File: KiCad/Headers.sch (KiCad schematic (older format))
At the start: 9 parts, among them CON601 AVR-JTAG-10, J601 ISP0, J602 ISP1, J603 CONN_01X02, J604 CONN_01X02, J605 CONN_01X02, J606 CONN_01X02, J607 CONN_01X03, J608 CONN_01X03

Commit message: More routing
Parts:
- CON601: footprint Pin_Headers:Pin_Header_Straight_2x06_Pitch2.54mm -> Pin_Headers:Pin_Header_Straight_2x05_Pitch2.54mm
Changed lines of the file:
@@
 F 0 "CON601" H 4424 1755 50  0000 C CNN
 F 1 "AVR-JTAG-10" H 4424 1664 50  0000 C CNN
-F 2 "Pin_Headers:Pin_Header_Straight_2x06_Pitch2.54mm" V 3880 1320 50  0001 C CNN
+F 2 "Pin_Headers:Pin_Header_Straight_2x05_Pitch2.54mm" V 3880 1320 50  0001 C CNN
 F 3 "" H 4450 1300 50  0001 C CNN
 	1    4450 1300

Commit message: Starting another routing pass
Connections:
- net GPIO/1UART0_TX renamed GPIO1/UART0_TX
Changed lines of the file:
@@
 $EndComp
 $Comp
-L GND #PWR0135
+L GND #PWR0133
 U 1 1 5924B01B
 P 4900 1500
-F 0 "#PWR0135" H 4900 1250 50  0001 C CNN
+F 0 "#PWR0133" H 4900 1250 50  0001 C CNN
 F 1 "GND" V 4905 1372 50  0000 R CNN
 F 2 "" H 4900 1500 50  0001 C CNN
@@
 NoConn ~ 4500 1400
 $Comp
-L GND #PWR0136
+L GND #PWR0134
 U 1 1 5924B02F
 P 4850 1100
-F 0 "#PWR0136" H 4850 850 50  0001 C CNN
+F 0 "#PWR0134" H 4850 850 50  0001 C CNN
 F 1 "GND" V 4855 972 50  0000 R CNN
 F 2 "" H 4850 1100 50  0001 C CNN
@@
 $EndComp
 $Comp
-L +3V3 #PWR0137
+L +3V3 #PWR0135
 U 1 1 5924B035
 P 4850 1200
-F 0 "#PWR0137" H 4850 1050 50  0001 C CNN
+F 0 "#PWR0135" H 4850 1050 50  0001 C CNN
 F 1 "+3V3" V 4865 1328 50  0000 L CNN
 F 2 "" H 4850 1200 50  0001 C CNN
@@
 GPIO17/UART2_TX
 Text GLabel 5450 2800 1    60   Input ~ 0
-GPIO/1UART0_TX
+GPIO1/UART0_TX
 Text GLabel 5300 2800 1    60   Input ~ 0
 GPIO3/UART0_RX
 $Comp
-L GND #PWR0138
+L GND #PWR0136
 U 1 1 59270647
 P 3050 2950
-F 0 "#PWR0138" H 3050 2700 50  0001 C CNN
+F 0 "#PWR0136" H 3050 2700 50  0001 C CNN
 F 1 "GND" V 3055 2822 50  0000 R CNN
 F 2 "" H 3050 2950 50  0001 C CNN
@@
 	3550 2600 3550 2950
 $Comp
-L GND #PWR0139
+L GND #PWR0137
 U 1 1 59270781
 P 3650 2950
-F 0 "#PWR0139" H 3650 2700 50  0001 C CNN
+F 0 "#PWR0137" H 3650 2700 50  0001 C CNN
 F 1 "GND" V 3655 2822 50  0000 R CNN
 F 2 "" H 3650 2950 50  0001 C CNN
@@
 	4150 2600 4150 2950
 $Comp
-L GND #PWR0140
+L GND #PWR0138
 U 1 1 59270905
 P 4250 2950
-F 0 "#PWR0140" H 4250 2700 50  0001 C CNN
+F 0 "#PWR0138" H 4250 2700 50  0001 C CNN
 F 1 "GND" V 4255 2822 50  0000 R CNN
 F 2 "" H 4250 2950 50  0001 C CNN
@@
 	4800 2600 4800 2950
 $Comp
-L GND #PWR0141
+L GND #PWR0139
 U 1 1 59270936
 P 4900 2950
-F 0 "#PWR0141" H 4900 2700 50  0001 C CNN
+F 0 "#PWR0139" H 4900 2700 50  0001 C CNN
 F 1 "GND" V 4905 2822 50  0000 R CNN
 F 2 "" H 4900 2950 50  0001 C CNN
@@
 $EndComp
 $Comp
-L GND #PWR0142
+L GND #PWR0140
 U 1 1 59271A0B
 P 5550 2950
-F 0 "#PWR0142" H 5550 2700 50  0001 C CNN
+F 0 "#PWR0140" H 5550 2700 50  0001 C CNN
 F 1 "GND" V 5555 2822 50  0000 R CNN
 F 2 "" H 5550 2950 50  0001 C CNN
@@
 	5900 2900 5900 2800
 $Comp
-L GND #PWR0143
+L GND #PWR0141
 U 1 1 59271B4E
 P 6150 2950
-F 0 "#PWR0143" H 6150 2700 50  0001 C CNN
+F 0 "#PWR0141" H 6150 2700 50  0001 C CNN
 F 1 "GND" V 6155 2822 50  0000 R CNN
 F 2 "" H 6150 2950 50  0001 C CNN

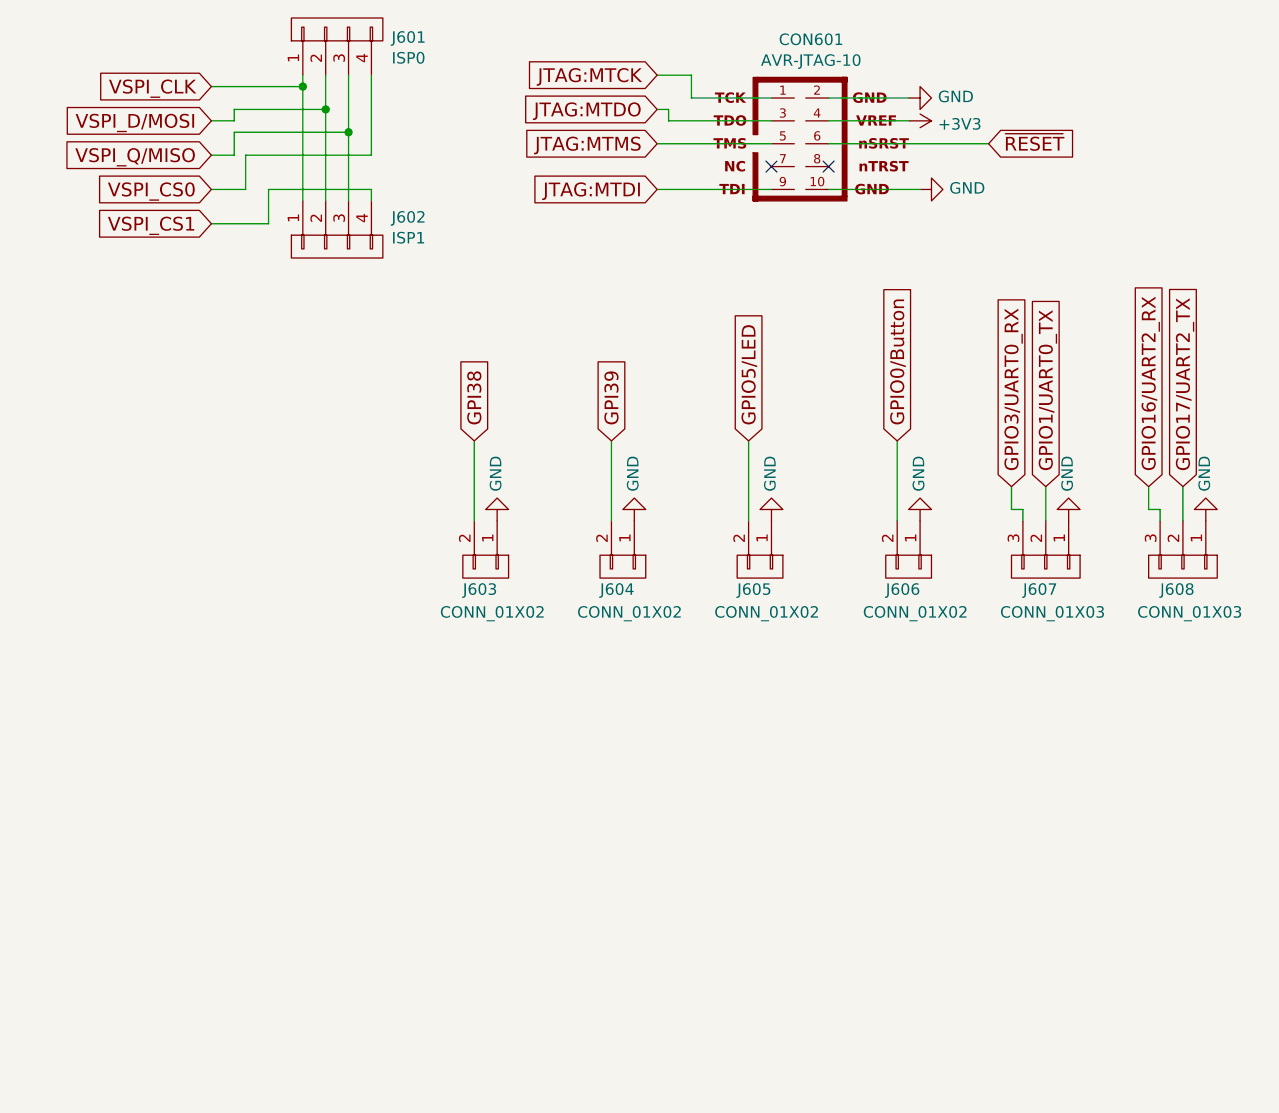
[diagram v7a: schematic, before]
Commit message: Added pullups for JTAG
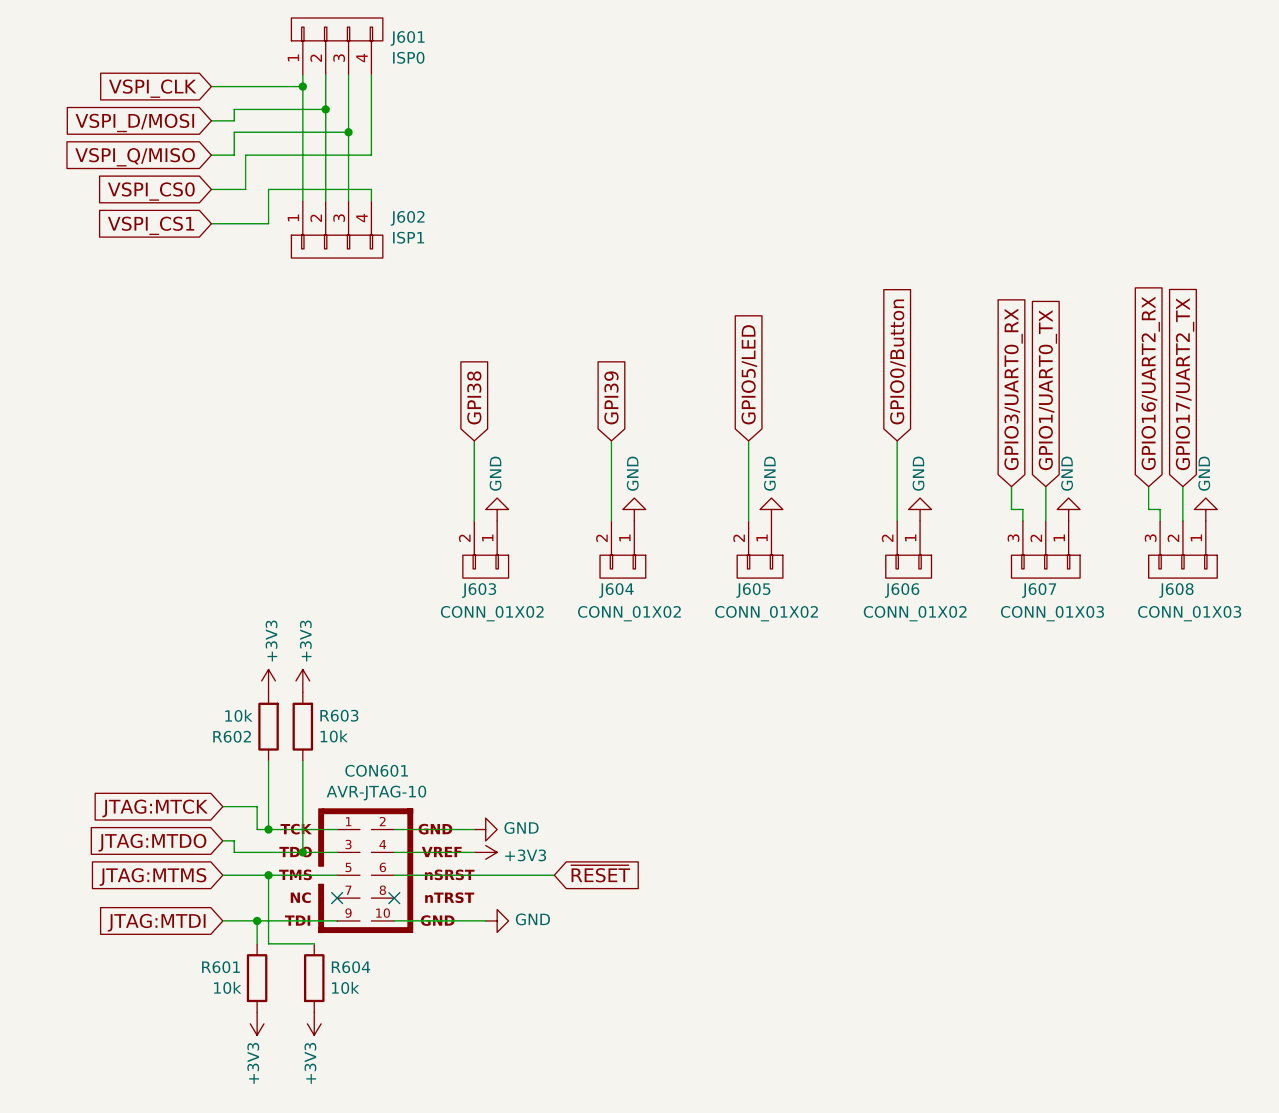
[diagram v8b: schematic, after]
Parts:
- added R601, R602, R603, R604: 10k, Resistors_SMD:R_0805, symbol R
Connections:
- net +3V3: now also R601.2, R602.2, R603.2, R604.2
- net JTAG:MTCK: now also R602.1
- net JTAG:MTDI: now also R601.1
- net JTAG:MTDO: now also R603.1
- net JTAG:MTMS: now also R604.1
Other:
- moved on the sheet: CON601
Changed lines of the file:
@@
 	0    -1   1    0
 $EndComp
-Text GLabel 3750 1500 0    60   Input ~ 0
+Text GLabel 1850 4700 0    60   Input ~ 0
 JTAG:MTDI
-Text GLabel 3750 1150 0    60   Input ~ 0
+Text GLabel 1850 4350 0    60   Input ~ 0
 JTAG:MTDO
-Text GLabel 3750 1000 0    60   Input ~ 0
+Text GLabel 1850 4200 0    60   Input ~ 0
 JTAG:MTCK
-Text GLabel 3750 1300 0    60   Input ~ 0
+Text GLabel 1850 4500 0    60   Input ~ 0
 JTAG:MTMS
-Text GLabel 5200 1300 2    60   Input ~ 0
+Text GLabel 3300 4500 2    60   Input ~ 0
 ~RESET
 $Comp
 L AVR-JTAG-10 CON601
 U 1 1 5924B014
-P 4450 1300
-F 0 "CON601" H 4424 1755 50  0000 C CNN
-F 1 "AVR-JTAG-10" H 4424 1664 50  0000 C CNN
-F 2 "Pin_Headers:Pin_Header_Straight_2x05_Pitch2.54mm" V 3880 1320 50  0001 C CNN
-F 3 "" H 4450 1300 50  0001 C CNN
-	1    4450 1300
-	1    0    0    -1
-$EndComp
-$Comp
-L GND #PWR0133
+P 2550 4500
+F 0 "CON601" H 2524 4955 50  0000 C CNN
+F 1 "AVR-JTAG-10" H 2524 4864 50  0000 C CNN
+F 2 "Pin_Headers:Pin_Header_Straight_2x05_Pitch2.54mm" V 1980 4520 50  0001 C CNN
+F 3 "" H 2550 4500 50  0001 C CNN
+	1    2550 4500
+	1    0    0    -1
+$EndComp
+$Comp
+L GND #PWR607
 U 1 1 5924B01B
-P 4900 1500
-F 0 "#PWR0133" H 4900 1250 50  0001 C CNN
-F 1 "GND" V 4905 1372 50  0000 R CNN
-F 2 "" H 4900 1500 50  0001 C CNN
-F 3 "" H 4900 1500 50  0001 C CNN
-	1    4900 1500
+P 3000 4700
+F 0 "#PWR607" H 3000 4450 50  0001 C CNN
+F 1 "GND" V 3005 4572 50  0000 R CNN
+F 2 "" H 3000 4700 50  0001 C CNN
+F 3 "" H 3000 4700 50  0001 C CNN
+	1    3000 4700
 	0    -1   -1   0
 $EndComp
-NoConn ~ 4250 1400
-NoConn ~ 4500 1400
-$Comp
-L GND #PWR0134
+NoConn ~ 2350 4600
+NoConn ~ 2600 4600
+$Comp
+L GND #PWR605
 U 1 1 5924B02F
-P 4850 1100
-F 0 "#PWR0134" H 4850 850 50  0001 C CNN
-F 1 "GND" V 4855 972 50  0000 R CNN
-F 2 "" H 4850 1100 50  0001 C CNN
-F 3 "" H 4850 1100 50  0001 C CNN
-	1    4850 1100
+P 2950 4300
+F 0 "#PWR605" H 2950 4050 50  0001 C CNN
+F 1 "GND" V 2955 4172 50  0000 R CNN
+F 2 "" H 2950 4300 50  0001 C CNN
+F 3 "" H 2950 4300 50  0001 C CNN
+	1    2950 4300
 	0    -1   -1   0
 $EndComp
 $Comp
-L +3V3 #PWR0135
+L +3V3 #PWR606
 U 1 1 5924B035
-P 4850 1200
-F 0 "#PWR0135" H 4850 1050 50  0001 C CNN
-F 1 "+3V3" V 4865 1328 50  0000 L CNN
-F 2 "" H 4850 1200 50  0001 C CNN
-F 3 "" H 4850 1200 50  0001 C CNN
-	1    4850 1200
+P 2950 4400
+F 0 "#PWR606" H 2950 4250 50  0001 C CNN
+F 1 "+3V3" V 2965 4528 50  0000 L CNN
+F 2 "" H 2950 4400 50  0001 C CNN
+F 3 "" H 2950 4400 50  0001 C CNN
+	1    2950 4400
 	0    1    1    0
 $EndComp
@@
 GPIO3/UART0_RX
 $Comp
-L GND #PWR0136
+L GND #PWR608
 U 1 1 59270647
 P 3050 2950
-F 0 "#PWR0136" H 3050 2700 50  0001 C CNN
+F 0 "#PWR608" H 3050 2700 50  0001 C CNN
 F 1 "GND" V 3055 2822 50  0000 R CNN
 F 2 "" H 3050 2950 50  0001 C CNN
@@
 	2500 1500 2500 1550
 Wire Wire Line
-	4500 1300 5200 1300
-Wire Wire Line
-	3900 1100 4250 1100
-Wire Wire Line
-	4500 1500 4900 1500
-Wire Wire Line
-	4850 1100 4500 1100
-Wire Wire Line
-	3750 1500 4250 1500
-Wire Wire Line
-	3750 1300 4250 1300
-Wire Wire Line
-	3800 1200 4250 1200
-Wire Wire Line
-	4850 1200 4500 1200
-Wire Wire Line
-	3900 1100 3900 1000
-Wire Wire Line
-	3900 1000 3750 1000
-Wire Wire Line
-	3800 1150 3750 1150
-Wire Wire Line
-	3800 1200 3800 1150
+	2600 4500 3300 4500
+Wire Wire Line
+	2000 4300 2350 4300
+Wire Wire Line
+	2600 4700 3000 4700
+Wire Wire Line
+	2950 4300 2600 4300
+Wire Wire Line
+	1850 4700 2350 4700
+Wire Wire Line
+	1850 4500 2350 4500
+Wire Wire Line
+	1900 4400 2350 4400
+Wire Wire Line
+	2950 4400 2600 4400
+Wire Wire Line
+	2000 4300 2000 4200
+Wire Wire Line
+	2000 4200 1850 4200
+Wire Wire Line
+	1900 4350 1850 4350
+Wire Wire Line
+	1900 4400 1900 4350
 Wire Wire Line
 	2950 2950 2950 2600
@@
 	3550 2600 3550 2950
 $Comp
-L GND #PWR0137
+L GND #PWR609
 U 1 1 59270781
 P 3650 2950
-F 0 "#PWR0137" H 3650 2700 50  0001 C CNN
+F 0 "#PWR609" H 3650 2700 50  0001 C CNN
 F 1 "GND" V 3655 2822 50  0000 R CNN
 F 2 "" H 3650 2950 50  0001 C CNN
@@
 	4150 2600 4150 2950
 $Comp
-L GND #PWR0138
+L GND #PWR610
 U 1 1 59270905
 P 4250 2950
-F 0 "#PWR0138" H 4250 2700 50  0001 C CNN
+F 0 "#PWR610" H 4250 2700 50  0001 C CNN
 F 1 "GND" V 4255 2822 50  0000 R CNN
 F 2 "" H 4250 2950 50  0001 C CNN
@@
 	4800 2600 4800 2950
 $Comp
-L GND #PWR0139
+L GND #PWR611
 U 1 1 59270936
 P 4900 2950
-F 0 "#PWR0139" H 4900 2700 50  0001 C CNN
+F 0 "#PWR611" H 4900 2700 50  0001 C CNN
 F 1 "GND" V 4905 2822 50  0000 R CNN
 F 2 "" H 4900 2950 50  0001 C CNN
@@
 $EndComp
 $Comp
-L GND #PWR0140
+L GND #PWR612
 U 1 1 59271A0B
 P 5550 2950
-F 0 "#PWR0140" H 5550 2700 50  0001 C CNN
+F 0 "#PWR612" H 5550 2700 50  0001 C CNN
 F 1 "GND" V 5555 2822 50  0000 R CNN
 F 2 "" H 5550 2950 50  0001 C CNN
@@
 	5900 2900 5900 2800
 $Comp
-L GND #PWR0141
+L GND #PWR613
 U 1 1 59271B4E
 P 6150 2950
-F 0 "#PWR0141" H 6150 2700 50  0001 C CNN
+F 0 "#PWR613" H 6150 2700 50  0001 C CNN
 F 1 "GND" V 6155 2822 50  0000 R CNN
 F 2 "" H 6150 2950 50  0001 C CNN
@@
 	-1   0    0    1
 $EndComp
+$Comp
+L R R601
+U 1 1 594046CD
+P 2000 4950
+F 0 "R601" H 1931 4996 50  0000 R CNN
+F 1 "10k" H 1931 4905 50  0000 R CNN
+F 2 "Resistors_SMD:R_0805" V 1930 4950 50  0001 C CNN
+F 3 "" H 2000 4950 50  0001 C CNN
+	1    2000 4950
+	1    0    0    -1
+$EndComp
+Wire Wire Line
+	2000 4800 2000 4700
+Connection ~ 2000 4700
+$Comp
+L +3V3 #PWR601
+U 1 1 5940481C
+P 2000 5100
+F 0 "#PWR601" H 2000 4950 50  0001 C CNN
+F 1 "+3V3" V 2015 5228 50  0000 L CNN
+F 2 "" H 2000 5100 50  0001 C CNN
+F 3 "" H 2000 5100 50  0001 C CNN
+	1    2000 5100
+	-1   0    0    1
+$EndComp
+$Comp
+L R R602
+U 1 1 59404845
+P 2050 3850
+F 0 "R602" H 2120 3896 50  0000 L CNN
+F 1 "10k" H 2120 3805 50  0000 L CNN
+F 2 "Resistors_SMD:R_0805" V 1980 3850 50  0001 C CNN
+F 3 "" H 2050 3850 50  0001 C CNN
+	1    2050 3850
+	-1   0    0    1
+$EndComp
+Wire Wire Line
+	2250 4800 2050 4800
+Wire Wire Line
+	2050 4800 2050 4500
+Connection ~ 2050 4500
+$Comp
+L +3V3 #PWR602
+U 1 1 59404923
+P 2050 3700
+F 0 "#PWR602" H 2050 3550 50  0001 C CNN
+F 1 "+3V3" V 2065 3828 50  0000 L CNN
+F 2 "" H 2050 3700 50  0001 C CNN
+F 3 "" H 2050 3700 50  0001 C CNN
+	1    2050 3700
+	1    0    0    -1
+$EndComp
+Wire Wire Line
+	2050 4000 2050 4300
+Connection ~ 2050 4300
+$Comp
+L R R603
+U 1 1 5940525E
+P 2200 3850
+F 0 "R603" H 2130 3804 50  0000 R CNN
+F 1 "10k" H 2130 3895 50  0000 R CNN
+F 2 "Resistors_SMD:R_0805" V 2130 3850 50  0001 C CNN
+F 3 "" H 2200 3850 50  0001 C CNN
+	1    2200 3850
+	-1   0    0    1
+$EndComp
+$Comp
+L +3V3 #PWR603
+U 1 1 59405264
+P 2200 3700
+F 0 "#PWR603" H 2200 3550 50  0001 C CNN
+F 1 "+3V3" V 2215 3828 50  0000 L CNN
+F 2 "" H 2200 3700 50  0001 C CNN
+F 3 "" H 2200 3700 50  0001 C CNN
+	1    2200 3700
+	1    0    0    -1
+$EndComp
+Wire Wire Line
+	2200 4000 2200 4400
+Connection ~ 2200 4400
+$Comp
+L R R604
+U 1 1 594059A5
+P 2250 4950
+F 0 "R604" H 2320 4996 50  0000 L CNN
+F 1 "10k" H 2320 4905 50  0000 L CNN
+F 2 "Resistors_SMD:R_0805" V 2180 4950 50  0001 C CNN
+F 3 "" H 2250 4950 50  0001 C CNN
+	1    2250 4950
+	1    0    0    -1
+$EndComp
+$Comp
+L +3V3 #PWR604
+U 1 1 594059AB
+P 2250 5100
+F 0 "#PWR604" H 2250 4950 50  0001 C CNN
+F 1 "+3V3" V 2265 5228 50  0000 L CNN
+F 2 "" H 2250 5100 50  0001 C CNN
+F 3 "" H 2250 5100 50  0001 C CNN
+	1    2250 5100
+	-1   0    0    1
+$EndComp
